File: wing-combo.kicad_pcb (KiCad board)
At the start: 2 copper layers, 93 x 91.3 mm, 114 parts, among them J1 Screw_Terminal_01x06, J13 USB_A, J15 Conn_01x16, J16 Conn_01x16, J17 Screw_Terminal_01x06, J18 Screw_Terminal_01x06, J3 Conn_01x12, J4 Conn_01x12, T1 AO3400A, T2 AO3400A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

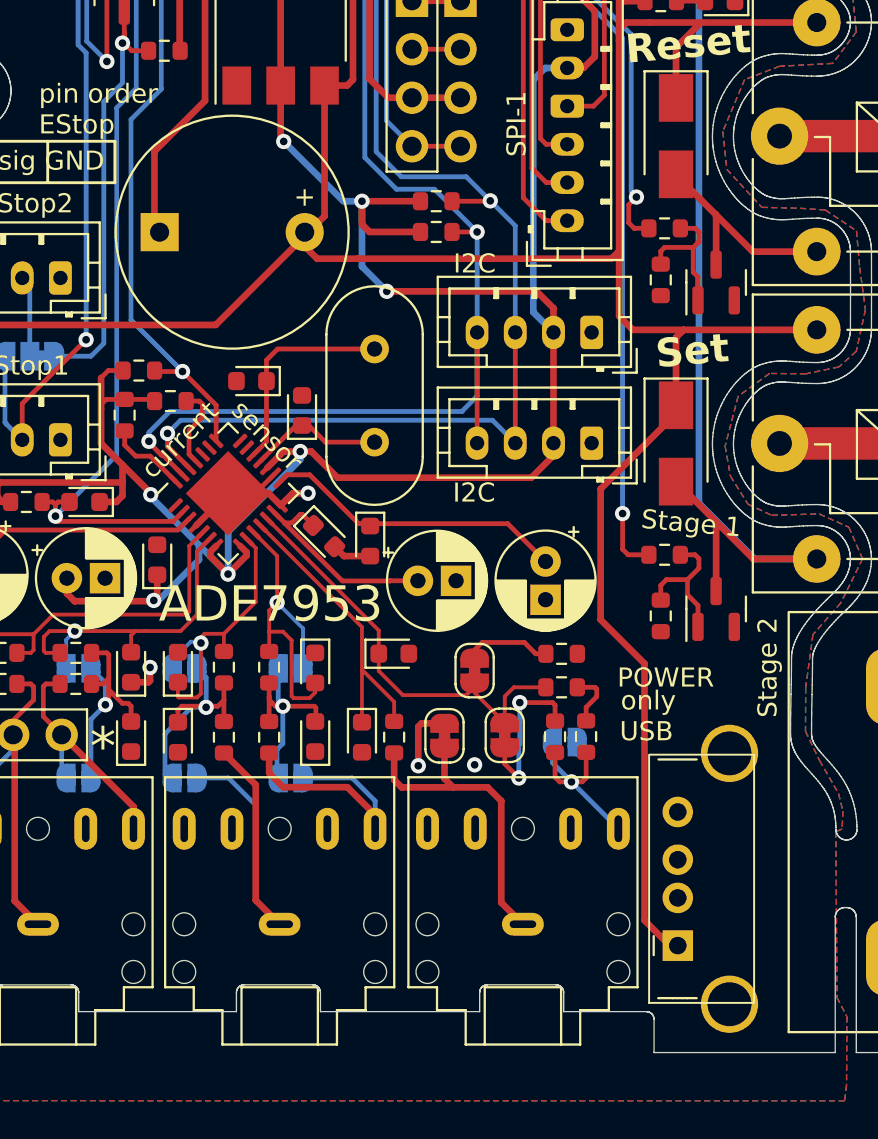
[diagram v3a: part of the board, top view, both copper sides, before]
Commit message: added 3D models to design
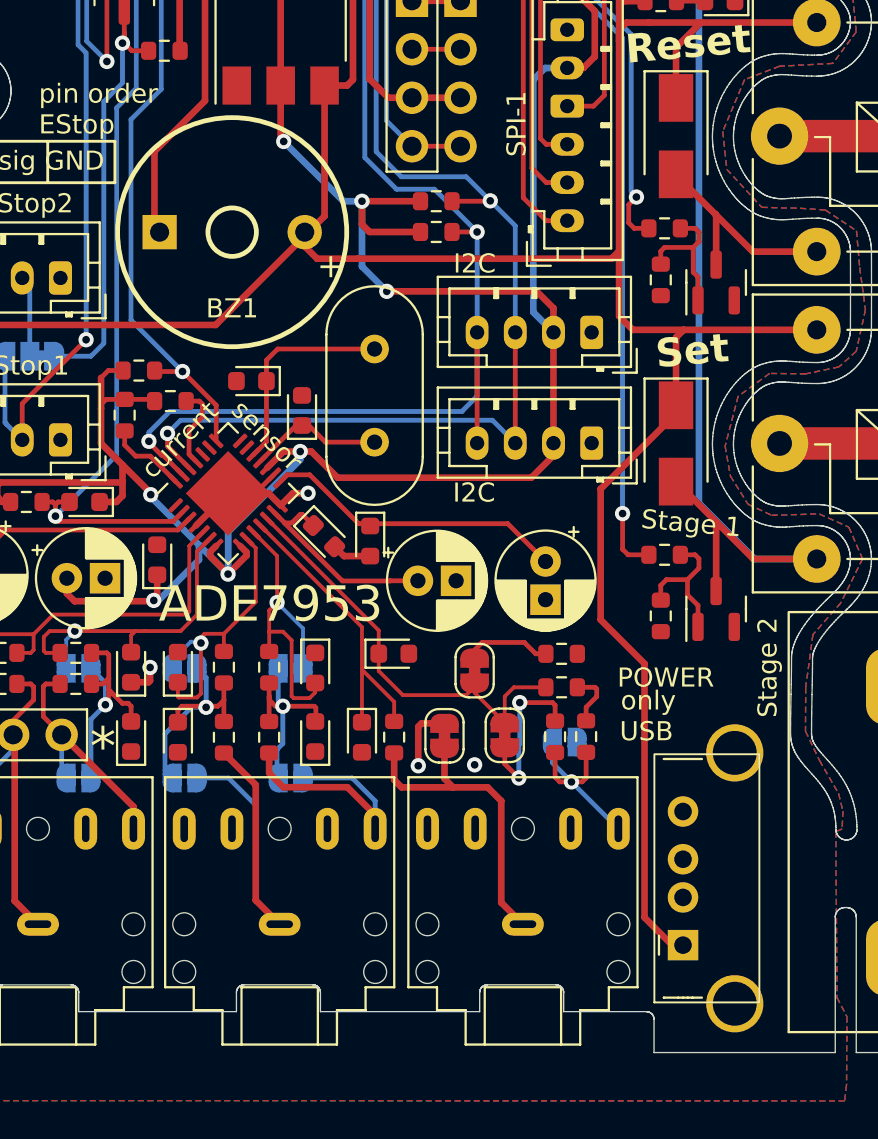
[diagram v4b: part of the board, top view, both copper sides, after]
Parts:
- BZ1: footprint Buzzer_Beeper:Buzzer_12x9.5RM7.6 -> buzzer:BUZ-TH_BD12.0-P7.60-D0.6-FD
- R31: value Relay_Omron_MY2-02 -> J1512CP120VAC
- moved J13 0.28 mm to (77.3, 108.5)
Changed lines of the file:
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@@
 	(footprint "Connector_USB:USB_A_Stewart_SS-52100-001_Horizontal"
 		(layer "F.Cu")
-		(at 77.015 108.57 90)
+		(at 77.29 108.545 90)
 		(descr "USB A connector https://belfuse.com/resources/drawings/stewartconnector/dr-stw-ss-52100-001.pdf")
 		(tags "USB_A Female Connector receptacle")
@@
 			)
 		)
+		(model "${KIPRJMOD}/odd-parts/usb-female/usb-female.3dshapes/USB-A-TH_L13.1-W5.7-H13.7-P2.0.step"
+			(offset
+				(xyz 3.5 -1.2 0)
+			)
+			(scale
+				(xyz 1 1 1)
+			)
+			(rotate
+				(xyz 0 0 0)
+			)
+		)
 	)
 	(footprint "Connector_JST:JST_PH_B2B-PH-K_1x02_P2.00mm_Vertical"
@@
 			)
 		)
-		(property "Value" "Relay_Omron_MY2-02"
+		(property "Value" "J1512CP120VAC"
 			(at 0 -6.5 90)
 			(unlocked yes)
@@
 			(pintype "passive")
 		)
-		(model "${EASYEDA2KICAD}/easyeda2kicad.3dshapes/CONN-TH_6P-P5.00_MX128-5.0-06P-GN01-CU-Y-A.wrl"
+		(model "${KIPRJMOD}/odd-parts/lcsc_screw_terminal/.3dshapes/CONN-TH_6P-P5.00_MX128-5.0-06P-GN01-CU-Y-A.wrl"
 			(offset
-				(xyz -0.3 -0.38 0)
+				(xyz 0 0 0)
 			)
 			(scale
@@
 			(pintype "passive")
 		)
-		(model "${EASYEDA2KICAD}/easyeda2kicad.3dshapes/CONN-TH_6P-P5.00_MX128-5.0-06P-GN01-CU-Y-A.wrl"
+		(model "${KIPRJMOD}/odd-parts/lcsc_screw_terminal/.3dshapes/CONN-TH_6P-P5.00_MX128-5.0-06P-GN01-CU-Y-A.wrl"
 			(offset
-				(xyz -0.3 -0.38 0)
+				(xyz 0 0 0)
 			)
 			(scale
@@
 			(pintype "power_out")
 		)
-		(model "CFM06S050-E.stp"
+		(model "${KIPRJMOD}/odd-parts/CFM06S050-E-Cincon/CFM06S050-E.stp"
 			(offset
 				(xyz 0 0 0)
@@
 		)
 	)
-	(footprint "Buzzer_Beeper:Buzzer_12x9.5RM7.6"
+	(footprint "buzzer:BUZ-TH_BD12.0-P7.60-D0.6-FD"
 		(layer "F.Cu")
 		(at 53.675 71.2 180)
-		(descr "Generic Buzzer, D12mm height 9.5mm with RM7.6mm")
-		(tags "buzzer")
 		(property "Reference" "BZ1"
-			(at 5.9944 4.0386 90)
+			(at 0 -4 180)
 			(layer "F.SilkS")
-			(hide yes)
 			(effects
 				(font
@@
 		)
 		(property "Value" "Buzzer"
-			(at 0 7.4 0)
+			(at 0 4 180)
 			(layer "F.Fab")
-			(hide yes)
 			(effects
 				(font
@@
 			)
 		)
-		(property "Footprint" "Buzzer_Beeper:Buzzer_12x9.5RM7.6"
+		(property "Footprint" "buzzer:BUZ-TH_BD12.0-P7.60-D0.6-FD"
 			(at 0 0 180)
-			(unlocked yes)
 			(layer "F.Fab")
 			(hide yes)
@@
 		(property "Datasheet" ""
 			(at 0 0 180)
-			(unlocked yes)
 			(layer "F.Fab")
 			(hide yes)
@@
 		(property "Description" ""
 			(at 0 0 180)
-			(unlocked yes)
 			(layer "F.Fab")
 			(hide yes)
@@
 		)
 		(property "JLCPCB Part #" "C96095"
-			(at 0 0 0)
+			(at 0 0 180)
+			(unlocked yes)
 			(layer "F.Fab")
 			(hide yes)
@@
 		(fp_circle
 			(center 0 0)
-			(end 6.1 0)
+			(end 6 0)
 			(stroke
-				(width 0.12)
+				(width 0.25)
 				(type solid)
 			)
@@
 		(fp_circle
 			(center 0 0)
-			(end 6.25 0)
+			(end 1.27 0)
 			(stroke
-				(width 0.05)
+				(width 0.25)
 				(type solid)
 			)
 			(fill none)
-			(layer "F.CrtYd")
+			(layer "F.SilkS")
 		)
 		(fp_circle
-			(center 0 0)
-			(end 6 0)
+			(center 3.8 0)
+			(end 3.95 0)
 			(stroke
-				(width 0.1)
+				(width 0.3)
 				(type solid)
 			)
@@
 		)
 		(fp_circle
-			(center 0 0)
-			(end 1 0)
+			(center -3.8 0)
+			(end -3.65 0)
 			(stroke
-				(width 0.1)
+				(width 0.3)
 				(type solid)
 			)
@@
 			(layer "F.Fab")
 		)
-		(fp_text user "+"
-			(at -3.8 1.85 0)
-			(layer "F.SilkS")
-			(effects
-				(font
-					(size 1 1)
-					(thickness 0.15)
-				)
+		(fp_circle
+			(center -6 6)
+			(end -5.97 6)
+			(stroke
+				(width 0.06)
+				(type solid)
 			)
+			(fill none)
+			(layer "F.Fab")
 		)
 		(fp_text user "+"
-			(at -3.81 -2.54 0)
-			(layer "F.Fab")
-			(hide yes)
+			(at -4.44 -1.77 180)
+			(layer "F.SilkS")
 			(effects
 				(font
-					(size 1 1)
+					(size 1.27 1.27)
 					(thickness 0.15)
 				)
+				(justify left)
 			)
 		)
 		(fp_text user "${REFERENCE}"
-			(at 0.0254 2.1844 0)
+			(at 0 0 180)
 			(layer "F.Fab")
 			(effects
@@
 		(pad "1" thru_hole circle
 			(at -3.8 0 180)
-			(size 2 2)
-			(drill 1)
+			(size 1.8 1.8)
+			(drill 0.999998)
 			(layers "*.Cu" "*.Mask")
 			(remove_unused_layers no)
@@
 		(pad "2" thru_hole rect
 			(at 3.8 0 180)
-			(size 2 2)
-			(drill 1)
+			(size 1.8 1.8)
+			(drill 0.999998)
 			(layers "*.Cu" "*.Mask")
 			(remove_unused_layers no)
@@
 			(pintype "passive")
 		)
-		(model "${KICAD6_3DMODEL_DIR}/Buzzer_Beeper.3dshapes/Buzzer_12x9.5RM7.6.wrl"
+		(model "/odd-parts/buzzer/.3dshapes/BUZ-TH_D12.0-H9.5-P7.60.wrl"
 			(offset
-				(xyz -3.8 0 0)
+				(xyz -0.02 -0 0)
 			)
 			(scale
-				(xyz 1 1 1)
+				(xyz 1 1 0.6)
 			)
 			(rotate
-				(xyz 0 0 0)
+				(xyz 0 0 -90)
 			)
 		)
@@
 			(pintype "passive")
 		)
-		(model "${EASYEDA2KICAD}/easyeda2kicad.3dshapes/CONN-TH_6P-P5.00_MX128-5.0-06P-GN01-CU-Y-A.wrl"
+		(model "${KIPRJMOD}/odd-parts/lcsc_screw_terminal/.3dshapes/CONN-TH_6P-P5.00_MX128-5.0-06P-GN01-CU-Y-A.wrl"
 			(offset
-				(xyz -0.3 -0.38 0)
+				(xyz 0 0 0)
 			)
 			(scale
@@
 	)
 	(segment
-		(start 76.925 80.7)
-		(end 76.925 80.2676)
+		(start 69.785 34.11)
+		(end 69.785 32.7)
 		(width 0.35)
 		(layer "F.Cu")
@@
 	)
 	(segment
-		(start 69.785 34.11)
-		(end 69.785 32.7)
+		(start 77.29 108.545)
+		(end 76.72 108.545)
 		(width 0.35)
 		(layer "F.Cu")
@@
 	)
 	(segment
-		(start 76.595 108.57)
-		(end 75.275 107.25)
-		(width 0.35)
-		(layer "F.Cu")
-		(net 3)
-	)
-	(segment
 		(start 75.525 60.2198)
 		(end 74.3239 60.2198)
@@
 	)
 	(segment
-		(start 73.9437 72.19)
-		(end 73.5437 72.59)
+		(start 75.275 93.8)
+		(end 72.975 91.5)
 		(width 0.35)
 		(layer "F.Cu")
@@
 	)
 	(segment
-		(start 73.9437 55.0453)
-		(end 75.595 53.394)
+		(start 73.9437 72.19)
+		(end 73.5437 72.59)
 		(width 0.35)
 		(layer "F.Cu")
@@
 	)
 	(segment
-		(start 72.975 84.65)
-		(end 76.925 80.7)
+		(start 73.9437 55.0453)
+		(end 75.595 53.394)
 		(width 0.35)
 		(layer "F.Cu")
@@
 	)
 	(segment
+		(start 76.72 108.545)
+		(end 75.275 107.1)
+		(width 0.35)
+		(layer "F.Cu")
+		(net 3)
+	)
+	(segment
 		(start 58.515 63.52)
 		(end 58.515 70.36)
@@
 	)
 	(segment
+		(start 75.275 107.1)
+		(end 75.275 93.8)
+		(width 0.35)
+		(layer "F.Cu")
+		(net 3)
+	)
+	(segment
 		(start 74.3239 60.2198)
 		(end 73.9437 60.6)
@@
 	)
 	(segment
-		(start 77.015 108.57)
-		(end 76.595 108.57)
-		(width 0.35)
-		(layer "F.Cu")
-		(net 3)
-	)
-	(segment
-		(start 72.975 91.5)
-		(end 72.975 84.65)
-		(width 0.35)
-		(layer "F.Cu")
-		(net 3)
-	)
-	(segment
 		(start 73.5437 72.59)
 		(end 60.255 72.59)
@@
 	)
 	(segment
+		(start 76.925 80.7)
+		(end 76.925 80.2676)
+		(width 0.35)
+		(layer "F.Cu")
+		(net 3)
+	)
+	(segment
 		(start 40.985 76.06)
 		(end 40.675 75.75)
@@
 	)
 	(segment
+		(start 72.975 91.5)
+		(end 72.975 84.65)
+		(width 0.35)
+		(layer "F.Cu")
+		(net 3)
+	)
+	(segment
+		(start 72.975 84.65)
+		(end 76.925 80.7)
+		(width 0.35)
+		(layer "F.Cu")
+		(net 3)
+	)
+	(segment
+		(start 77.265 108.57)
+		(end 77.29 108.545)
+		(width 0.35)
+		(layer "F.Cu")
+		(net 3)
+	)
+	(segment
 		(start 73.9437 61.2)
 		(end 73.9437 60.6)
@@
 	)
 	(segment
-		(start 75.275 93.8)
-		(end 72.975 91.5)
-		(width 0.35)
-		(layer "F.Cu")
-		(net 3)
-	)
-	(segment
 		(start 50.925 55.29)
 		(end 50.925 61.675)
 		(width 0.35)
 		(layer "F.Cu")
-		(net 3)
-	)
-	(segment
-		(start 75.275 107.25)
-		(end 75.275 93.8)
-		(width 0.35)
-		(layer "F.Cu")

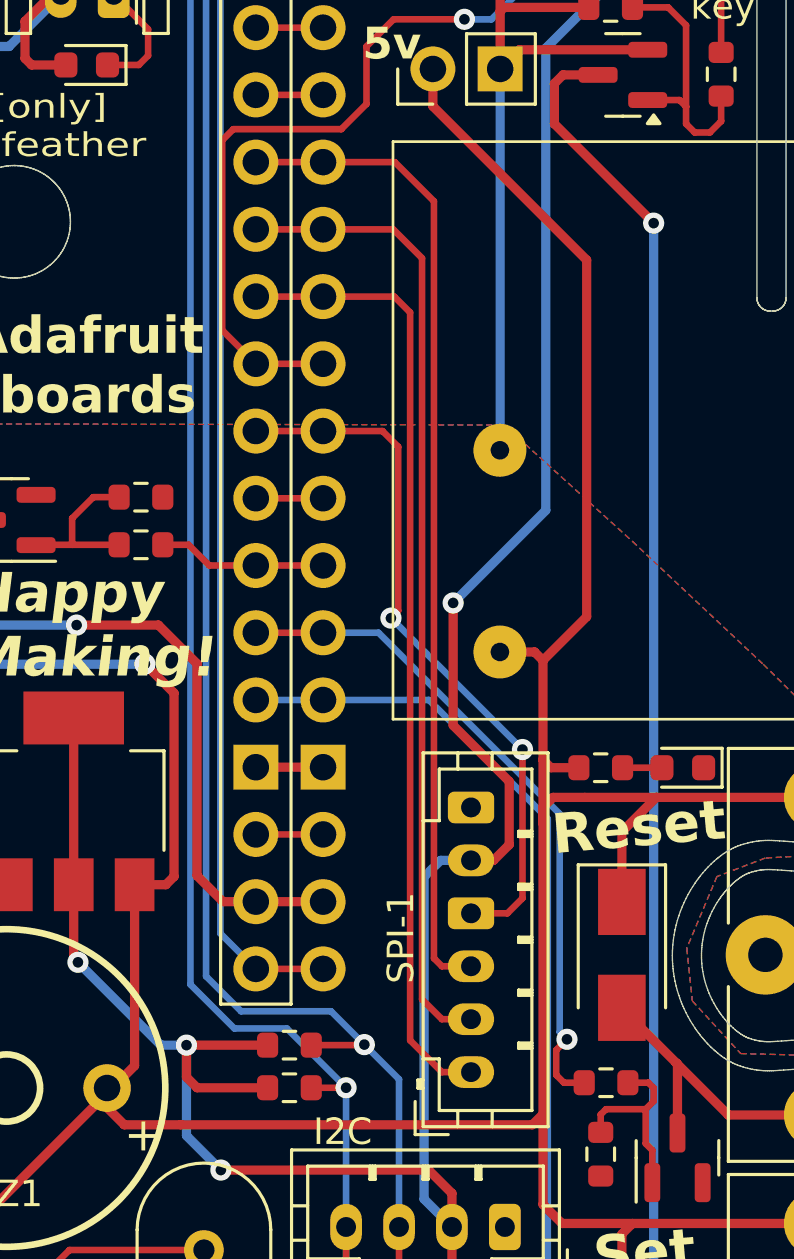
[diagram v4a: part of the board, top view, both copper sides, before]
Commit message: [fix] PICO/POCI flipped on Feather Boards
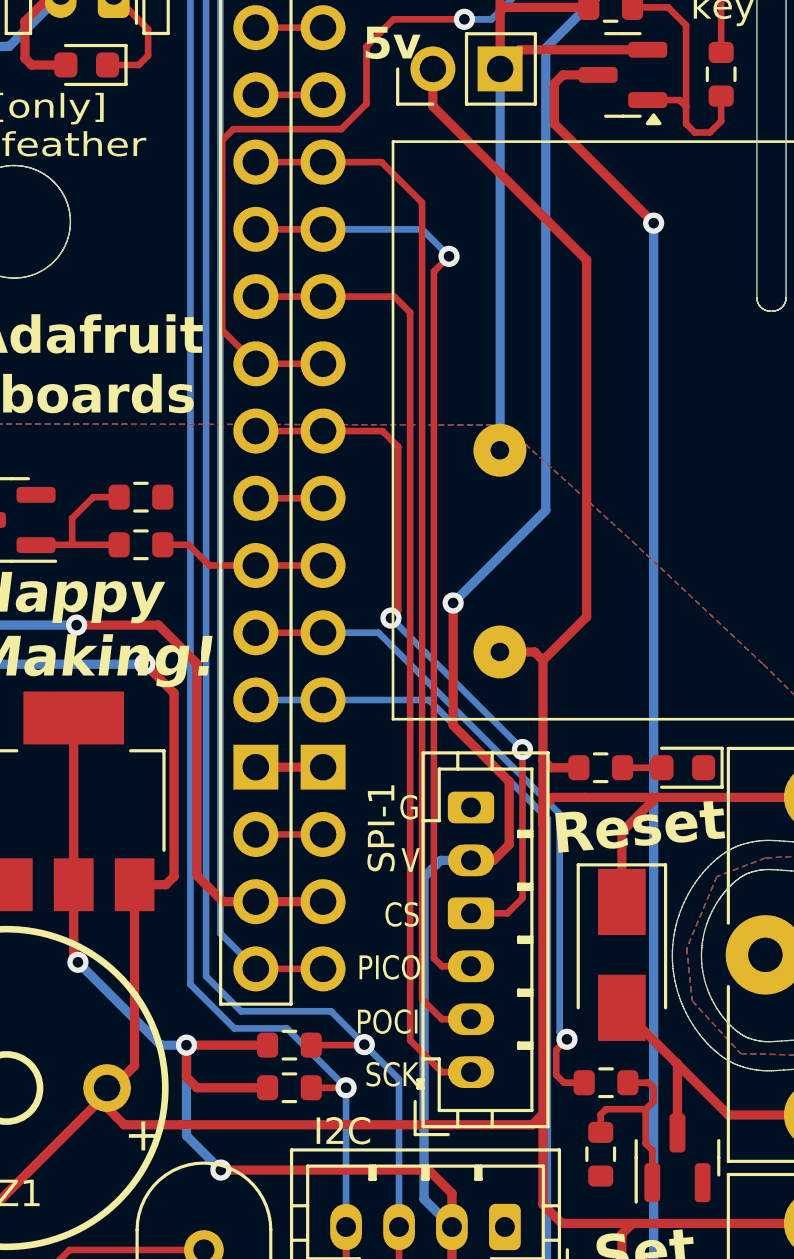
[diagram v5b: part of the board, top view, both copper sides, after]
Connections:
- J15 pad 4: PICO -> POCI
- J15 pad 5: POCI -> PICO
- J16 pad 4: PICO -> POCI
- J16 pad 5: POCI -> PICO
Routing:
- net POCI: track 36.9 -> 39.2 mm
- net PICO: track 37.5 -> 36.0 mm, vias 0 -> 1
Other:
- board text added: "CS"
- board text added: "G"
- board text added: "PICO"
- board text added: "POCI"
- board text added: "SCK"
- board text added: "V"
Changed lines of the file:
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@@
 			(layers "*.Cu" "*.Mask")
 			(remove_unused_layers no)
-			(net 37 "PICO")
+			(net 38 "POCI")
 			(pinfunction "Pin_4")
 			(pintype "passive")
@@
 			(layers "*.Cu" "*.Mask")
 			(remove_unused_layers no)
-			(net 38 "POCI")
+			(net 37 "PICO")
 			(pinfunction "Pin_5")
 			(pintype "passive")
@@
 		(tags "connector JST PH side entry")
 		(property "Reference" "SPI-1"
-			(at 5.07 -2.65 -90)
+			(at 9.23 -3.36 -90)
 			(layer "F.SilkS")
 			(effects
@@
 			(layers "*.Cu" "*.Mask")
 			(remove_unused_layers no)
-			(net 37 "PICO")
+			(net 38 "POCI")
 			(pinfunction "Pin_4")
 			(pintype "passive")
@@
 			(layers "*.Cu" "*.Mask")
 			(remove_unused_layers no)
-			(net 38 "POCI")
+			(net 37 "PICO")
 			(pinfunction "Pin_5")
 			(pintype "passive")
@@
 		)
 	)
+	(gr_text "G"
+		(at 69.295 61.15 0)
+		(layer "F.SilkS")
+		(effects
+			(font
+				(size 0.9 0.75)
+				(thickness 0.1)
+			)
+			(justify right bottom)
+		)
+	)
 	(gr_text "Stage 2"
 		(at 81.725 94 90)
@@
 		)
 	)
+	(gr_text "CS"
+		(at 69.305 65.2 0)
+		(layer "F.SilkS")
+		(effects
+			(font
+				(size 0.9 0.75)
+				(thickness 0.1)
+			)
+			(justify right bottom)
+		)
+	)
 	(gr_text "Fits all Adafruit \nFeather boards"
 		(at 44.275 45.85 0)
@@
 		)
 	)
+	(gr_text "SCK"
+		(at 69.255 71.24 0)
+		(layer "F.SilkS")
+		(effects
+			(font
+				(size 0.9 0.75)
+				(thickness 0.1)
+			)
+			(justify right bottom)
+		)
+	)
 	(gr_text "EStp1"
 		(at 125.345 108.720001 90)
@@
 		)
 	)
+	(gr_text "V"
+		(at 69.295 63.15 0)
+		(layer "F.SilkS")
+		(effects
+			(font
+				(size 0.9 0.75)
+				(thickness 0.1)
+			)
+			(justify right bottom)
+		)
+	)
 	(gr_text "stage 1 "
 		(at 127.225 38.6 90)
@@
 		)
 	)
+	(gr_text "POCI"
+		(at 69.305 69.25 0)
+		(layer "F.SilkS")
+		(effects
+			(font
+				(size 0.9 0.75)
+				(thickness 0.1)
+			)
+			(justify right bottom)
+		)
+	)
 	(gr_text "current"
 		(at 50.935 82.08 45)
@@
 		)
 	)
+	(gr_text "PICO"
+		(at 69.365 67.2 0)
+		(layer "F.SilkS")
+		(effects
+			(font
+				(size 0.9 0.75)
+				(thickness 0.1)
+			)
+			(justify right bottom)
+		)
+	)
 	(gr_text "Reset"
 		(at 77.565 61.35 5)
@@
 	)
 	(segment
-		(start 70.125 66.6)
-		(end 69.825 66.3)
+		(start 65.635 38.76)
+		(end 63.095 38.76)
 		(width 0.25)
 		(layer "F.Cu")
@@
 	)
 	(segment
-		(start 71.225 66.6)
+		(start 69.825 66.3)
 		(end 70.125 66.6)
 		(width 0.25)
@@
 	)
 	(segment
-		(start 69.825 37.7)
-		(end 68.345 36.22)
+		(start 70.395 39.78)
+		(end 69.825 40.35)
 		(width 0.25)
 		(layer "F.Cu")
@@
 	)
 	(segment
-		(start 65.635 36.22)
-		(end 63.095 36.22)
+		(start 69.825 40.35)
+		(end 69.825 66.3)
 		(width 0.25)
 		(layer "F.Cu")
@@
 	)
 	(segment
-		(start 69.825 66.3)
-		(end 69.825 37.7)
+		(start 70.125 66.6)
+		(end 71.225 66.6)
 		(width 0.25)
 		(layer "F.Cu")
 		(net 37)
 	)
+	(via
+		(at 70.395 39.78)
+		(size 0.8)
+		(drill 0.4)
+		(layers "F.Cu" "B.Cu")
+		(net 37)
+	)
 	(segment
-		(start 68.345 36.22)
-		(end 65.635 36.22)
+		(start 69.375 38.76)
+		(end 70.395 39.78)
 		(width 0.25)
-		(layer "F.Cu")
+		(layer "B.Cu")
 		(net 37)
 	)
 	(segment
-		(start 69.375 39.85)
-		(end 68.285 38.76)
+		(start 65.635 38.76)
+		(end 69.375 38.76)
 		(width 0.25)
-		(layer "F.Cu")
-		(net 38)
+		(layer "B.Cu")
+		(net 37)
 	)
 	(segment
-		(start 65.635 38.76)
-		(end 63.095 38.76)
+		(start 67.845 36.22)
+		(end 65.635 36.22)
 		(width 0.25)
 		(layer "F.Cu")
@@
 	)
 	(segment
-		(start 71.225 68.6)
-		(end 70.125 68.6)
+		(start 69.375 37.75)
+		(end 67.845 36.22)
+		(width 0.25)
+		(layer "F.Cu")
+		(net 38)
+	)
+	(segment
+		(start 65.635 36.22)
+		(end 63.095 36.22)
 		(width 0.25)
 		(layer "F.Cu")
@@
 	(segment
 		(start 69.375 67.85)
-		(end 69.375 39.85)
+		(end 69.375 37.75)
 		(width 0.25)
 		(layer "F.Cu")
@@
 	)
 	(segment
-		(start 68.285 38.76)
-		(end 65.635 38.76)
+		(start 71.225 68.6)
+		(end 70.125 68.6)
 		(width 0.25)
 		(layer "F.Cu")
